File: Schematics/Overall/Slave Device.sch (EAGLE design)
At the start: 26 parts, among them J1 POWER_JACK

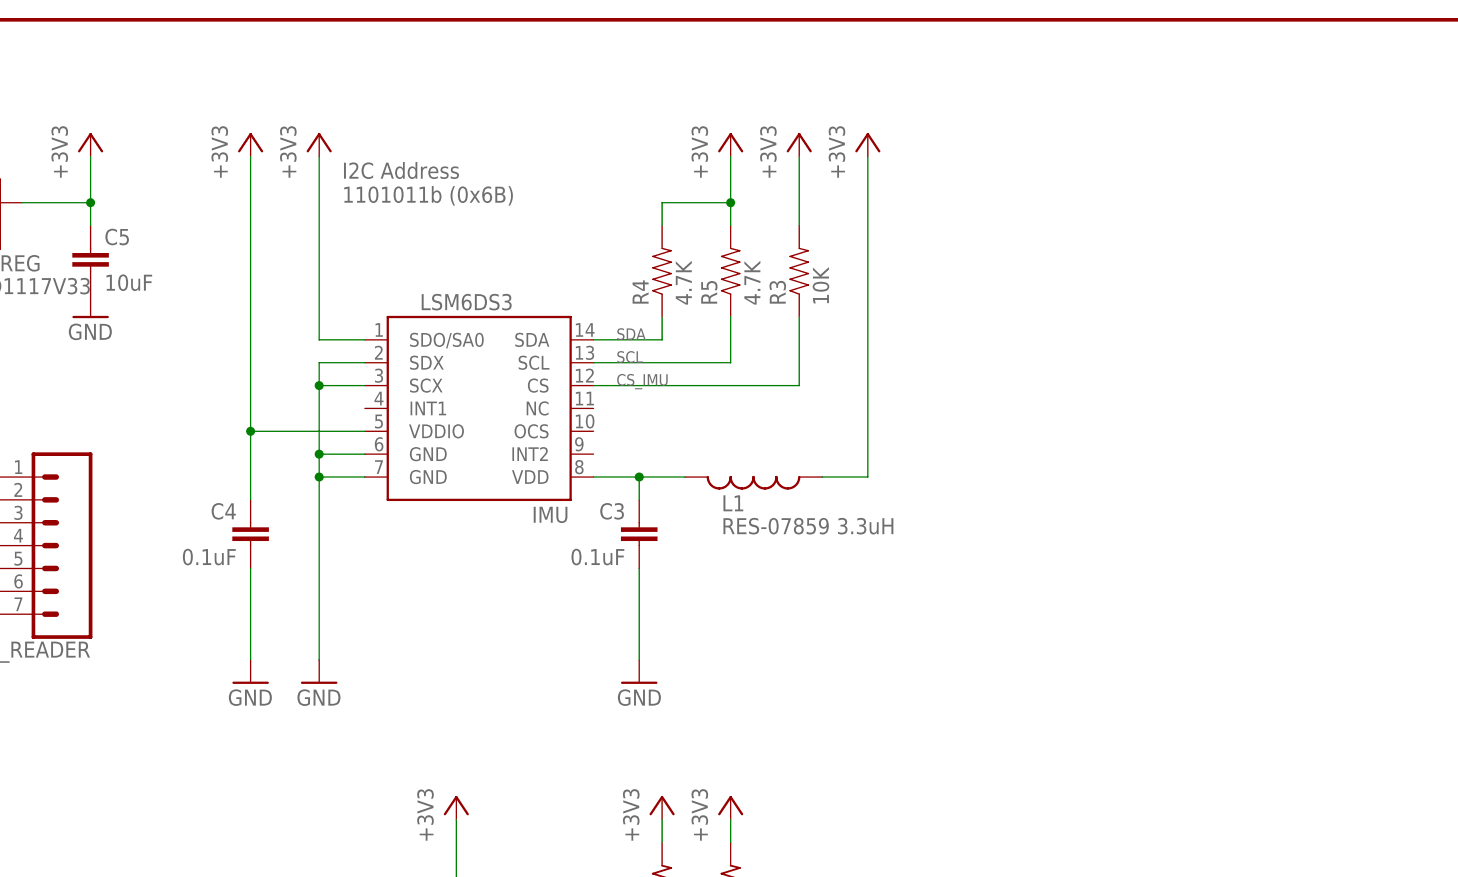
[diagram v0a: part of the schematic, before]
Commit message: Updated Master with battery sensor
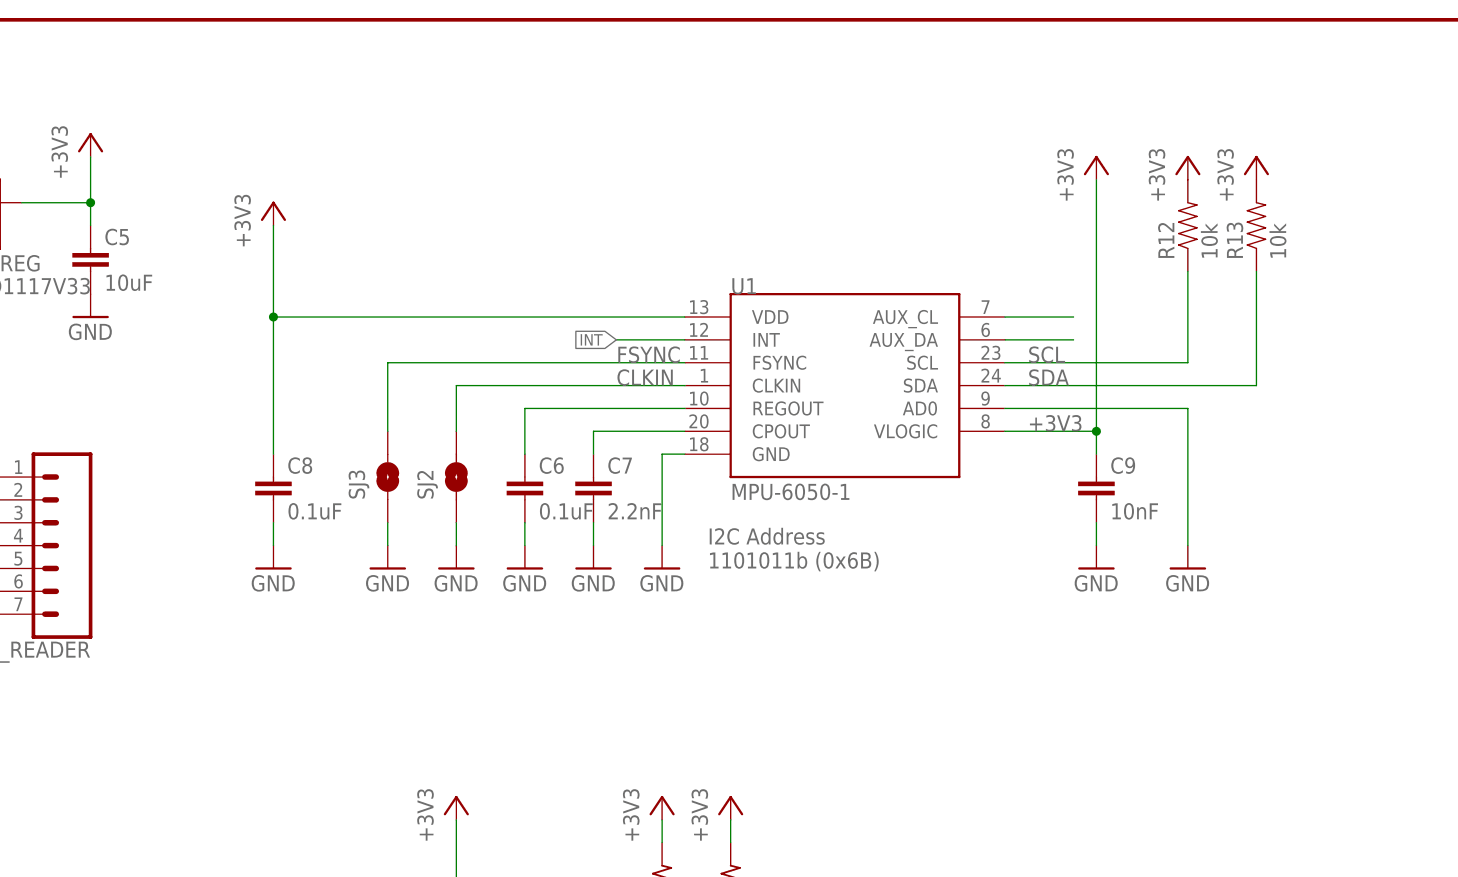
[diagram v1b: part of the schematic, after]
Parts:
- removed C3, C4: 0.1uF, SparkFun-Capacitors:0.1UF-100V-10%(0603)
- removed IMU: LSM6DS3, LSM6DS3:LSM6DS3DOT_INDICATION
- removed L1: RES-07859 3.3uH, SparkFun-Passives:INDUCTOR30OHM,1.8A
- removed R3: 10K, SparkFun-Resistors:10KOHM-1/10W-1%(0603)0603
- removed R4, R5: 4.7K, SparkFun-Resistors:4.7KOHM-1/10W-1%(0603)
- added C6, C8: 0.1uF, SparkFun:CAP0603-CAP
- added C7: 2.2nF, SparkFun:CAP0603-CAP
- added C9: 10nF, SparkFun:CAP0603-CAP
- added R12, R13: 10k, SparkFun:RESISTOR0603-RES
- added SJ2, SJ3: SOLDERJUMPERTRACE, SparkFun:SOLDERJUMPERTRACE
- added U1: MPU-6050-1, Testing:MPU-6050-1
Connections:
- removed net CS_IMU: IMU.CS, R3.1
- removed net VDD: C3.1, IMU.VDD, L1.2
- new net AUX_SCL: U1.AUX_CL
- new net AUX_SDA: U1.AUX_DA
- new net CLKIN: SJ2.2, U1.CLKIN
- new net FSYNC: SJ3.2, U1.FSYNC
- new net INT: U1.INT
- new net N$10: C6.1, U1.REGOUT
- new net N$9: C7.1, U1.CPOUT
- net +3V3: now also C8.1, C9.1, R12.2, R13.2, U1.VDD, U1.VLOGIC; no longer C4.1, IMU.SDO/SA0, IMU.VDDIO, L1.1, R3.2, R4.2, R5.2
- net GND: now also C6.2, C7.2, C8.2, C9.2, SJ2.1, SJ3.1, U1.AD0, U1.GND; no longer C3.2, C4.2, IMU.GND@6, IMU.GND@7, IMU.SCX, IMU.SDX
- net SCL: now also R12.1, U1.SCL; no longer IMU.SCL, R5.1
- net SDA: now also R13.1, U1.SDA; no longer IMU.SDA, R4.1

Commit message: Finalized Schematics
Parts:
- removed D2: RED, SparkFun-LED:LED3MM
- added C3: 10uF, SparkFun:CAP0603-CAP
- added C4: (no value), rcl:C-US050-050X075
- added D3: RED, SparkFun-LED:LED3MM
- added FSR1, FSR2: (no value), SparkFun-Connectors:CONN_02
- added MPU_BO: (no value), SparkFun-Connectors:CONN_05
- added NMOS: STN3NF06L, STN3NF06L:STN3NF06L
- added R15: 68 Ohm, SparkFun-Resistors:68OHM-0603-1/10W-1%
- added R3: 20k, SparkFun-Resistors:10KOHM-1/10W-1%(0603)0603
- added R4: 500, SparkFun-Resistors:10KOHM-1/10W-1%(0603)0603
- added R5: 6k, SparkFun-Resistors:10KOHM-1/10W-1%(0603)0603
- C1, C2: device SparkFun-Capacitors:0.1UF-KIT-EZ-50V-20% -> SparkFun:CAP0603-CAP
- C5: value 10uF -> (none); device SparkFun-Capacitors:10UF-1206-6.3V-20% -> rcl:C-US050-050X075
- R10, R11: value 20K -> 4k; device resistor:R-US_0411/15 -> SparkFun-Resistors:10KOHM-1/10W-1%(0603)0603
- R2: value 68 Ohm -> 4k; device SparkFun-Resistors:68OHM-0603-1/10W-1% -> SparkFun-Resistors:10KOHM-1/10W-1%(0603)0603
- R8: value FSR -> 4k; device resistor:R-US_0204/5 -> SparkFun-Resistors:10KOHM-1/10W-1%(0603)0603
- R9: value FSR -> 12k; device resistor:R-US_0204/5 -> SparkFun-Resistors:10KOHM-1/10W-1%(0603)0603
- RESET: value MOMENTARY-SWITCH-SPST-PTH-6.0MM -> PTH-RIGHT; device SparkFun-Switches:MOMENTARY-SWITCH-SPST-PTH-6.0MM -> SparkFun-Switches:MOMENTARY-SWITCH-SPST-PTH-RIGHT-ANGLE-KIT
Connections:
- removed net AUX_SCL: U1.AUX_CL
- removed net AUX_SDA: U1.AUX_DA
- removed net INT: U1.INT
- new net 9V_BAT: C1.1, J1.PWR, R9.2, V_REG.IN
- new net MPU_INT: MICROCONTROLLER.PD2(INT0), MPU_BO.1, U1.INT
- new net N$11: NMOS.1, R4.1
- new net N$12: NMOS.2, R5.1
- new net N$14: FSR2.2, R11.2, R8.2
- new net SENSE: MICROCONTROLLER.PC2(ADC2), R5.2, R9.1
- new net V_MON: MICROCONTROLLER.PD4(XCK/T0), R3.2, R4.2
- net +3V3: now also C2.1, C3.1, FSR1.1, FSR2.1, MPU_BO.5; no longer C5.1, R8.2, R9.2
- net FSR1: now also C4.1, R10.1; no longer R10.2, R8.1
- net FSR2: now also C5.1, R11.1; no longer R11.2, R9.1
- net GND: now also C3.2, C4.2, D1.C, D3.C, MPU_BO.4, NMOS.3, R3.1, R8.1, RESET.1; no longer C2.1, R1.1, R10.1, R11.1, RESET.2
- net N$2: now also MICROCONTROLLER.PD3(INT1), RESET.2; no longer MICROCONTROLLER.PD2(INT0), RESET.1
- net N$4: now also R1.2; no longer D2.A
- net N$5: now also R15.2; no longer D1.A
- net N$6: now also D3.A, R15.1; no longer D1.C, R1.2
- net N$7: now also D1.A, R1.1; no longer D2.C, R2.2
- net N$8: now also FSR1.2, R10.2, R2.2; no longer C1.1, J1.PWR, V_REG.IN
- net SCL: now also MPU_BO.2
- net SDA: now also MPU_BO.3
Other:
- moved on the sheet: C5, D1, R1, R10, R11, R2, R6, R8, R9, RESET
